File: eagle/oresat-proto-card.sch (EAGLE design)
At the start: 126 parts, among them J1 J-SAMTEC-TFM-110-X1-XXX-D-RA, J2 U.FL, J3 U.FL, J4 U.FL, J6 J-SAMTEC-TFM-120-X1-XXX-D-RA, J7 ORESAT-DEBUG-CONNECTOR-SOLAR, Q1 DMP2240UDM, Q3 MOSFET-PCH-SOT23-6, Q4 MOSFET-PCH-SOT23-6, Q5 PMV45EN, Q6 PMV45EN, U1 TCAN330, U3 MAX7310ATE, U4 MAX4211FETE, U5 TPS62111RSA, U7 STM32F091C, U8 MIC842LYC5, U9 MIC842LYC5, X2 16MHZ-2.5x2mm

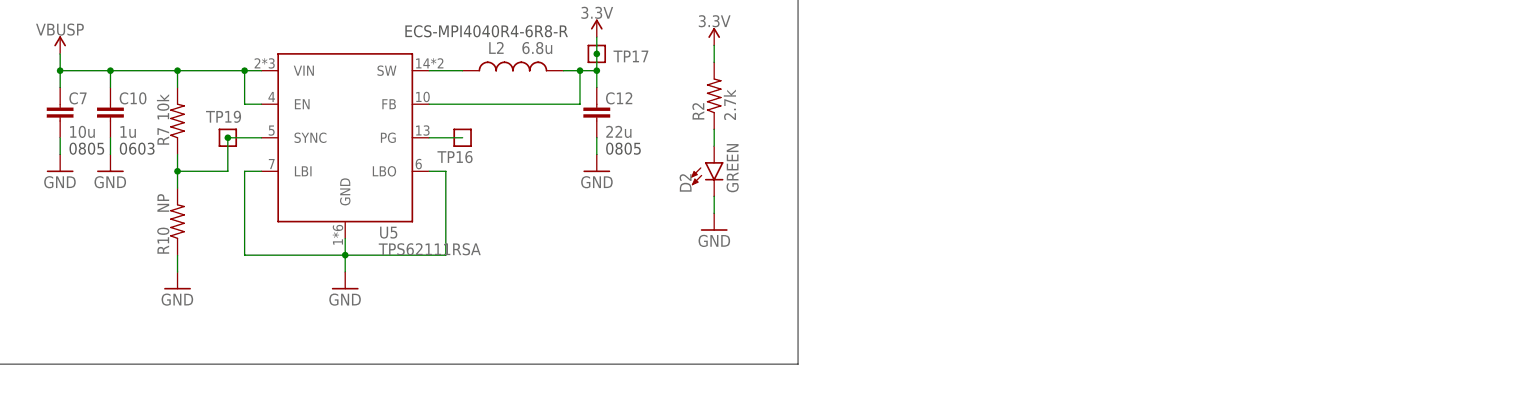
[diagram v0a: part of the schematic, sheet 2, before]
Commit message: swapped 0402 to 0603 where necessary, fixed labels on tnames layer
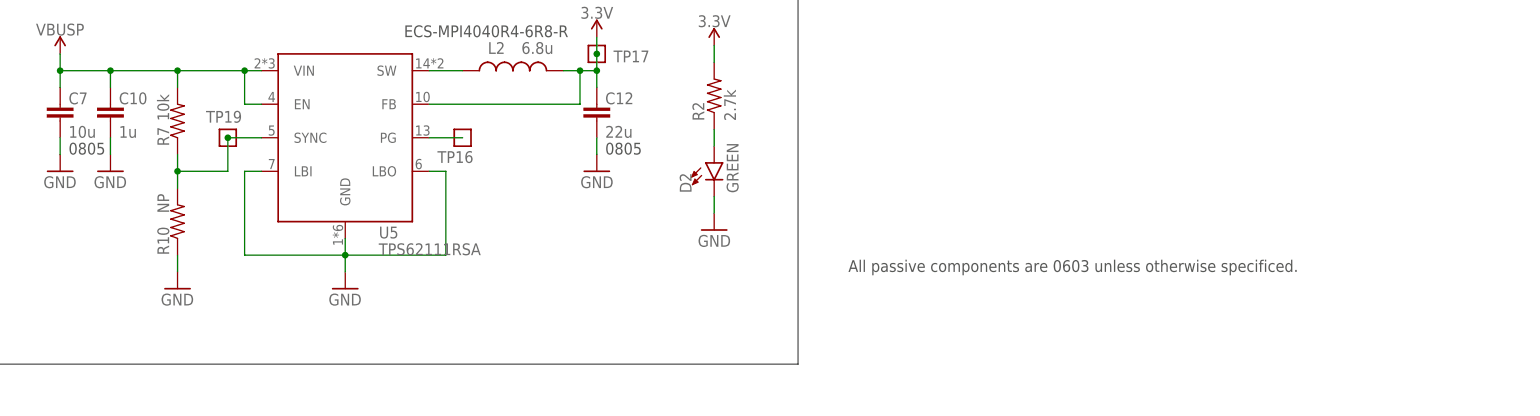
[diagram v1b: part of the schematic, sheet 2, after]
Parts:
- C1, C2: device rcl_custom:C-EU0402-B-NOSILK -> oresat-rcl:C-EU0603-C-NOSILK
- C4, C5, C6: device oresat-rcl:C-EU0603-B-NOSILK -> oresat-rcl:C-EU0603-C-NOSILK
- R10, R11, R12, R13, R14, R15, R16, R18, R19, R20, R21, R22, R23, R25, R26, R27, R28, R30, R31, R32, R33, R34, R35, R36, R37, R38, R39, R40, R41, R42, R43, R44, R5, R6, R7, R8, R9: device rcl_custom:R-US_0402-B-NOSILK -> oresat-rcl:R-US_0603-C-NOSILK
- R29: device rcl:R-US_R1206 -> oresat-rcl:R-US_0603-C-NOSILK
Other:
- note added: "All passive components are 0603 unless otherwise specificed."
- note added: "TODO:Replace attributes of passives with 0603"

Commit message: updated design blocks, got rid of unneeded breakouts
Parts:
- removed C1: 100n, oresat-rcl:C-EU0603-C-NOSILK
- removed C10: 1u, oresat-rcl:C-EU0603-B-NOSILK
- removed C12: 22u, oresat-rcl:C-EU0805-B-NOSILK
- removed C2: NP, oresat-rcl:C-EU0603-C-NOSILK
- removed C4, C5, C6: 1u, oresat-rcl:C-EU0603-C-NOSILK
- removed C7: 10u, oresat-rcl:C-EU0805-B-NOSILK
- removed D1, D2: GREEN, SparkFun-LED:LED-GREEN0603
- removed D4: AMBER, SparkFun-LED:LED-GREEN0603
- removed JP1: (no value), pinhead:PINHD-1X6
- removed JP3: (no value), pinhead:PINHD-1X3
- removed JP5, JP6: (no value), pinhead:PINHD-1X5
- removed JP7: (no value), pinhead:PINHD-2X10
- removed L2: 6.8u, L-ECS-MPI4040:L-ECS-MPI4040
- removed Q1: DMP2240UDM, Q-MOSFET-PCH-dual-SOT23-6:MOSFET-PCH-SOT23-6
- removed Q3, Q4: MOSFET-PCH-SOT23-6, Q-MOSFET-PCH-SOT23-6:MOSFET-PCH-SOT23-6
- removed Q5, Q6: PMV45EN, Tova:PMV45EN
- removed R1, R12, R2: 2.7k, oresat-rcl:R-US_0603-C-NOSILK
- removed R10, R11, R14, R19, R20, R22, R23, R32, R34, R36, R37, R5, R8, R9: NP, oresat-rcl:R-US_0603-C-NOSILK
- removed R15, R26, R27, R28, R30, R35, R38, R42, R7: 10k, oresat-rcl:R-US_0603-C-NOSILK
- removed R16, R43: 330k, oresat-rcl:R-US_0603-C-NOSILK
- removed R18, R44: 1M, oresat-rcl:R-US_0603-C-NOSILK
- removed R25, R41: 100, oresat-rcl:R-US_0603-C-NOSILK
- removed R29: 100m, oresat-rcl:R-US_0603-C-NOSILK
- removed R31, R33: 0, oresat-rcl:R-US_0603-C-NOSILK
- removed R4: 100, rcl_custom:R-US_0402-B-NOSILK
- removed TP1, TP10, TP11, TP12, TP13, TP14, TP16, TP17, TP18, TP19, TP20, TP22, TP3, TP5, TP6, TP7, TP8, TP9: TEST-POINT, Tova:TEST-POINT
- removed U3: MAX7310ATE, U-Maxim-MAX7310-I2C-GPIO-expander:MAX7310
- removed U4: MAX4211FETE, U-Maxim-MAX4211-power-monitor:MAX4211
- removed U5: TPS62111RSA, U-TI-TPS6211x-SPS-buck:TPS6211X
- removed U8, U9: MIC842LYC5, U-Microchip-MIC842-Comparator:MIC842LYC5
- added C11, C17, C22, C23: 1u, oresat-rcl:C-EU0603-C-NOSILK
- added C16: 22u, oresat-rcl:C-EU0805-B-NOSILK
- added C3: 100n, oresat-rcl:C-EU0603-C-NOSILK
- added C8: NP, oresat-rcl:C-EU0603-C-NOSILK
- added C9: 10u, oresat-rcl:C-EU0805-B-NOSILK
- added D3, D6: GREEN, SparkFun-LED:LED-GREEN0603
- added D7: AMBER, SparkFun-LED:LED-GREEN0603
- added JP11, JP8: (no value), pinhead:PINHD-2X10
- added L1: 6.8u, L-ECS-MPI4040:L-ECS-MPI4040
- added Q10: DMP2240UDM, Q-MOSFET-PCH-dual-SOT23-6:MOSFET-PCH-SOT23-6
- added Q2, Q7: MOSFET-PCH-SOT23-6, Q-MOSFET-PCH-SOT23-6:MOSFET-PCH-SOT23-6
- added Q8, Q9: PMV45EN, Tova:PMV45EN
- added R17, R3, R76: 2.7k, oresat-rcl:R-US_0603-C-NOSILK
- added R24: 10, oresat-rcl:R-US_0603-C-NOSILK
- added R46, R52, R53, R55, R56, R57, R59, R67, R69, R71, R72, R75: NP, oresat-rcl:R-US_0603-C-NOSILK
- added R60, R80: 100, oresat-rcl:R-US_0603-C-NOSILK
- added R61, R62, R63, R65, R70, R73, R74, R77, R81: 10k, oresat-rcl:R-US_0603-C-NOSILK
- added R64: 100m, rcl:R-US_R1206
- added R66, R68: 0, oresat-rcl:R-US_0603-C-NOSILK
- added R78, R82: 330k, oresat-rcl:R-US_0603-C-NOSILK
- added R79, R83: 1M, oresat-rcl:R-US_0603-C-NOSILK
- added TP15, TP2, TP21, TP23, TP24, TP33, TP34, TP35, TP36, TP37, TP38, TP39, TP4, TP40, TP41, TP42: TEST-POINT-LARGE-SQUARE, oresat-misc:TEST-POINT-LARGE-SQUARE
- added TP25: TEST-POINT, Tova:TEST-POINT
- added U10: TPS62111RSA, U-TI-TPS6211x-SPS-buck:TPS6211X
- added U11, U12: MIC842LYC5, U-Microchip-MIC842-Comparator:MIC842LYC5
- added U2: MAX7310ATE, U-Maxim-MAX7310-I2C-GPIO-expander:MAX7310
- added U6: MAX4211FETE, U-Maxim-MAX4211-power-monitor:MAX4211
- R39, R40: value 47k -> NP; DPN 311-47.0KLRCT-ND -> 1276-4275-1-ND; MFR Yageo -> Samsung; MPN RC0402FR-0747KL -> RC1005F6653CS
- TP31, TP32: value TEST-POINT -> TEST-POINT-LARGE-SQUARE; device Tova:TEST-POINT -> oresat-misc:TEST-POINT-LARGE-SQUARE
- renumbered R13 to R54, R21 to R58, R6 to R45
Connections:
- removed net CAN_SILENT: U1.S, U7.PA9
- removed net IOUT: R31.2, U4.IOUT
- removed net MAX4211-3V3: C5.1, TP10.1, U3.IO7, U4.VCC
- removed net N$270: D1.A, R1.1
- removed net N$271: D2.A, R2.1
- removed net N$385: R39.1, R40.1, TP5.1, U3.IO6
- removed net N$398: Q3.S, R29.2, R35.2, U4.RS-
- removed net N$400: C6.1, R43.1, R44.1, U8.INP
- removed net N$401: C4.1, R16.1, R18.1, U9.INP
- removed net N$479: Q1.2.S, R41.2
- removed net N$480: Q1.2.G, R42.2, TP22.1, U8.OUT
- removed net N$527: J7.SWO, TP32.1
- removed net N$575: D4.A, R12.1
- removed net N$579: Q1.1.S, R25.2
- removed net N$580: Q1.1.G, R15.2, TP7.1, U9.OUT
- removed net N$589: R26.1, U3.!RESET
- removed net N$590: Q4.G, Q5.D, R27.1
- removed net N$593: Q4.D, R29.1, U4.RS+
- removed net N$596: R31.1, R32.2, TP12.1, U4.CIN1+
- removed net N$597: R33.1, R34.2, TP11.1, U4.CIN1-
- removed net N$599: R33.2, U4.CIN2+, U4.REF
- removed net N$603: C2.1, R36.2, R37.2
- removed net N$604: R37.1, U4.INHIBIT
- removed net POUTPROT: JP7.13, R49.2, U7.PA8
- removed net TPS62111-PG: TP16.1, U5.PG
- removed net TPS62111-SYNC: R10.2, R7.1, TP19.1, U5.SYNC
- removed net TPS62111_SW: L2.1, U5.SW
- new net IOUT1: R66.2, U6.IOUT
- new net N$518: D3.A, R3.1
- new net N$519: D6.A, R17.1
- new net N$520: R61.1, U2.!RESET
- new net N$522: J7.DEBUG-3, TP29.1
- new net N$529: Q7.G, Q8.D, R62.1
- new net N$530: Q7.D, R64.1, U6.RS+
- new net N$531: R66.1, R67.2, TP15.1, U6.CIN1+
- new net N$532: R68.1, R69.2, TP4.1, U6.CIN1-
- new net N$533: R68.2, U6.CIN2+, U6.REF
- new net N$534: R72.1, U6.INHIBIT
- new net N$535: C8.1, R71.2, R72.2
- new net N$536: Q2.S, R64.2, R70.2, U6.RS-
- new net N$537: D7.A, R76.1
- new net N$538: Q10.1.S, R60.2
- new net N$539: Q10.1.G, R77.2, TP41.1, U12.OUT
- new net N$540: TP40.1, U2.IO6
- new net N$541: Q10.2.S, R80.2
- new net N$573: Q10.2.G, R81.2, TP42.1, U11.OUT
- new net N$574: C23.1, R82.1, R83.1, U11.INP
- new net N$578: C22.1, R78.1, R79.1, U12.INP
- new net N$581: TP36.1, U2.IO7
- new net PA8/POUTPROT: JP8.6, R49.2, U7.PA8
- new net PA9/CAN_SILENT: JP8.8, U1.S, U7.PA9
- new net PB10: JP11.10, U7.PB10
- new net PB11: JP11.12, U7.PB11
- new net PB12: JP11.14, U7.PB12
- new net PB13: JP11.16, U7.PB13
- new net PB14: JP11.18, U7.PB14
- new net PB15: JP11.20, U7.PB15
- new net PB2: JP11.13, U7.PB2
- new net PB8: JP11.6, U7.PB8
- new net PB9: JP11.8, U7.PB9
- new net PC13: JP8.1, U7.PC13
- new net PC14: JP8.3, U7.PC14-OSC32_IN
- new net PC15: JP8.5, U7.PC15-OSC32_OUT
- new net TPS62111-PG1: TP32.1, U10.PG
- new net TPS62111-SYNC1: R74.1, R75.2, TP33.1, U10.SYNC
- new net TPS62111_SW3: L1.1, U10.SW
- net !FAULT: now also Q9.D, R73.1, TP24.1, U2.IO2; no longer Q6.D, R38.1, TP8.1, U3.IO2
- net !SD: no longer JP1.3
- net 3.3V: now also C16.1, L1.2, R17.2, TP34.1, U10.FB; no longer C12.1, JP1.4, JP5.1, JP5.2, JP5.3, JP5.4, JP5.5, JP6.1, JP6.2, JP6.3, JP6.4, JP6.5, L2.2, R2.2, TP17.1, U5.FB
- net AD0: now also R39.1, R40.2, R46.1, U2.AD0; no longer R5.1, R8.2, R9.1, U3.AD0
- net AD1: now also R52.1, R53.2, R55.1, U2.AD1; no longer R11.1, R14.2, R19.1, U3.AD1
- net AD2: now also R56.1, R57.2, R59.1, U2.AD2; no longer R20.1, R22.2, R23.1, U3.AD2
- net BOOT0: now also JP11.3, TP25.1, U2.IO5; no longer TP26.1, U3.IO5
- net CAN1_H: no longer JP1.1
- net CAN1_L: no longer JP1.2
- net CAN_RX: now also JP8.12
- net CAN_SHDN: now also JP8.10
- net CAN_TX: now also JP8.14
- net CB-RESET: now also R65.2, TP23.1, U2.IO4, U6.CIN2-; no longer R30.2, TP14.1, U3.IO4, U4.CIN2-
- net CB_CTRL: now also Q2.G, Q9.G, R70.1, TP39.1, U6.COUT1, U6.COUT2, U6.LE; no longer Q3.G, Q6.G, R35.1, TP3.1, U4.COUT1, U4.COUT2, U4.LE
- net GND: now also C11.2, C16.2, C17.2, C22.2, C23.2, C3.1, C9.2, D3.C, D6.C, D7.C, JP8.19, Q8.S, Q9.S, R45.1, R54.1, R58.1, R63.1, R65.1, R67.1, R69.1, R71.1, R75.1, R77.1, R81.1, U10.GND, U10.LBI, U10.LBO, U11.GND, U12.GND, U2.GND, U6.GND; no longer C1.1, C10.2, C12.2, C4.2, C5.2, C6.2, C7.2, D1.C, D2.C, D4.C, JP1.6, JP7.15, JP7.17, JP7.19, Q5.S, Q6.S, R10.1, R14.1, R15.1, R22.1, R28.1, R30.1, R32.1, R34.1, R36.1, R42.1, R8.1, U3.GND, U4.GND, U5.GND, U5.LBI, U5.LBO, U8.GND, U9.GND
- net N$523: now also J7.DEBUG-2, TP28.1; no longer J7.DEBUG-3, TP31.1
- net N$524: now also J7.DEBUG-1, TP27.1; no longer J7.DEBUG-2, TP30.1
- net N$525: now also J7.DEBUG-0, TP26.1; no longer J7.DEBUG-1, TP29.1
- net N$526: now also J7.SWO, TP30.1; no longer J7.DEBUG-0, TP28.1
- net NRESET: now also JP11.1; no longer TP27.1
- net ON/!OFF: now also C17.1, Q8.G, R63.2, R76.2, TP21.1, U2.IO3, U6.VCC; no longer Q5.G, R12.2, R28.2, TP13.1, U3.IO3
- net OPD_PWR: now also R24.1; no longer R4.1
- net OPD_SCL: now also R80.1; no longer R41.1
- net OPD_SDA: now also R60.1; no longer R25.1
- net PA0: now also JP8.7; no longer JP7.2
- net PA1: now also JP8.9; no longer JP7.4
- net PA15: now also JP8.16; no longer JP7.11
- net PA2/USART2_TX: now also JP8.11; no longer JP7.6
- net PA3/USART2_RX: now also JP8.13; no longer JP7.8
- net PA4: now also JP8.15; no longer JP7.10
- net PA5/SPI1_SCK: now also JP8.17; no longer JP7.12
- net PA6/SPI1_MISO: now also JP8.2; no longer JP7.14
- net PA7/SPI1_MOSI: now also JP8.4; no longer JP7.16
- net PB0: now also JP11.9; no longer JP7.18
- net PB1: now also JP11.11; no longer JP7.20
- net PB3: now also JP11.15; no longer JP7.9
- net PB4: now also JP11.17; no longer JP7.7
- net PB5: now also JP11.19; no longer JP7.5
- net PB6/SCL: now also JP11.2, U2.IO0; no longer JP7.3, R40.2, U3.IO0
- net PB7/SDA: now also JP11.4, U2.IO1; no longer JP7.1, R39.2, U3.IO1
- net PEN-SCL-FILT: now also Q10.2.D, R40.1, R53.1, R57.1, R82.2, TP37.1, U2.SCL; no longer Q1.2.D, R43.2, R45.1, R54.1, R58.1, TP18.1, U3.SCL
- net PEN-SDA-FILT: now also Q10.1.D, R46.2, R55.2, R59.2, R78.2, TP38.1, U2.SDA; no longer Q1.1.D, R16.2, R19.2, R23.2, R9.2, TP20.1, U3.SDA
- net POUT: now also TP2.1, U6.POUT; no longer TP6.1, U4.POUT
- net SWCLK: now also JP11.7
- net SWDIO: now also JP11.5
- net VBUS: now also Q7.S, R62.2; no longer Q4.S, R27.2
- net VBUSP: now also C11.1, C8.2, C9.1, Q2.D, R3.2, R74.2, TP31.1, U10.EN, U10.VIN; no longer C10.1, C2.2, C7.1, JP1.5, JP3.1, JP3.2, JP3.3, Q3.D, R1.2, R7.2, TP9.1, U5.EN, U5.VIN
- net VPD: now also C3.2, R24.2, R39.2, R52.2, R56.2, R61.2, R73.2, R79.2, R83.2, TP35.1, U11.VDD, U12.VDD, U2.V+; no longer C1.2, R11.2, R18.2, R20.2, R26.2, R38.2, R4.2, R44.2, R5.2, TP1.1, U3.V+, U8.VDD, U9.VDD
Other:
- note added: "1206"
- note added: "GPIO Breakouts"
- note added: "Rx-Tx switch happens on programming board"
- note added: "TODO: Replace with part in OreSat-Eagle Repo"
- note added: "VBAT not bypassed becase not enough room instead tied into nearest bypass cap"
- note removed: "0603"
- note removed: "47k forces slow I2C"
- note removed: "Place only if I2C pullups not placed."
- note removed: "Rx-Tx flip happens on proramming board"
- note removed: "TODO:Replace attributes of passives with 0603"
- note removed: "Vbat not bypassed because no space on layout tied to nearest bypass cap instead"

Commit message: Polishing to the schematic only; ready for v4! Still needs layout polishing.
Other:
- note added: "3.4"
- note added: "4.0"
- note added: "All caps are 0603 ceramic 10% X5R Vw>=16V unless marked"
- note added: "All resistors 0603 +/- 1% unless marked"
- note removed: "3.1"
- note removed: "All caps are 0402 ceramic 10% X5R Vw>=16V unless marked"
- note removed: "All resistors 0402 +/- 1% unless marked"
- note removed: "TODO: Replace with part in OreSat-Eagle Repo"
- moved on the sheet: C19, R48, U1

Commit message: moved ffc to bottom of card, fixed silkscreen, moved and expanded Vbus and 3.3V breakouts
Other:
- note added: "All caps are 0402 ceramic 10% X5R Vw>=16V unless marked"
- note added: "All caps are ceramic 10% X5R >= 16V V unless marked"
- note added: "All resistors 0402 +/- 1% unless marked"
- note removed: "3.4"
- note removed: "All caps are 0603 ceramic 10% X5R Vw>=16V unless marked"
- note removed: "All passive components are 0603 unless otherwise specificed."
- note removed: "Each VDD pin bypassed"
- moved on the sheet: C19, R48, U1

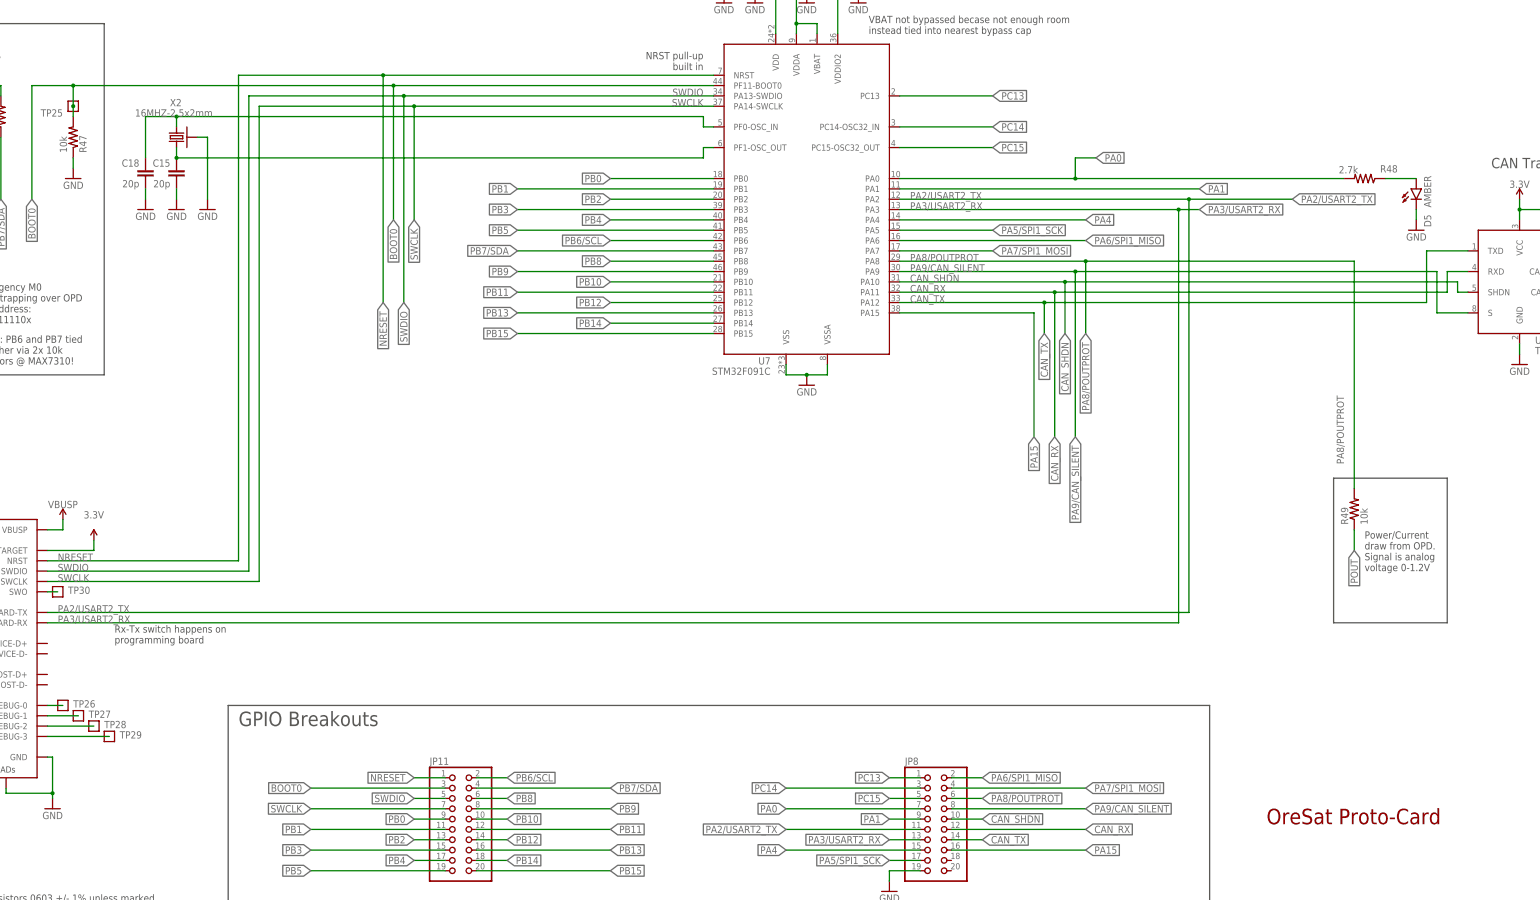
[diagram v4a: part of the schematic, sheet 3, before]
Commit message: fixed an error where Pout was not routed to an ADC pin
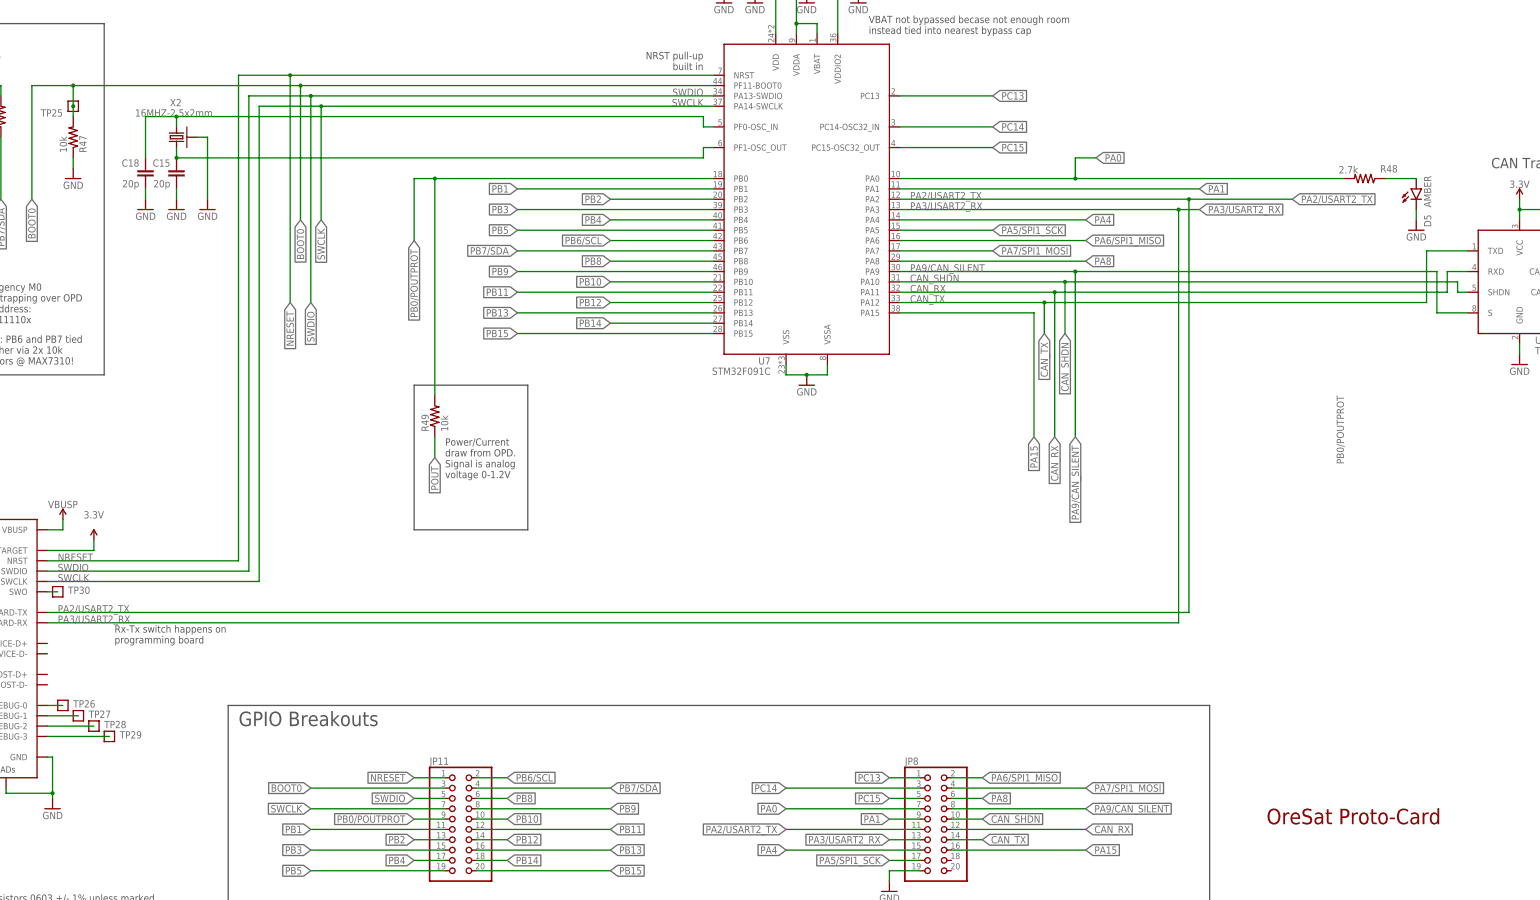
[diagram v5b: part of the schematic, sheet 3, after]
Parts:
- C11, C17, C22, C23: DPN 311-1446-1-ND -> 311-1444-1-ND; MPN CC0603KRX7R7BB105 -> CC0603KRX5R7BB105
- C3: DPN 1276-1001-1-ND -> 399-14941-1-ND; MFR Samsung -> Kemet; MPN CL05B104KO5NNNC -> C0603C104K4PAC7867
- R17, R3, R76: DPN A129632CT-ND -> P2.7KDBCT-ND; MFR TE Connectivity -> Panasonic; MPN CRGCQ0402F2K7 -> ERA-3AEB272V
- R24: DPN 311-100LRCT-ND -> 311-10.0HRCT-ND; MPN RC0402FR-07100RL -> RC0603FR-0710RL
- R60, R80: DPN 311-100LRCT-ND -> 311-100HRCT-ND; MPN RC0402FR-07100RL -> RC0603FR-07100RL
- R61, R62, R63, R65, R70, R73, R74, R77, R81: DPN 311-10.0KLRCT-ND -> RNCP0603FTD10K0CT-ND; MFR Yageo -> Stackpole; MPN RC0402FR-0710KL -> RNCP0603FTD10K0
- R66, R68: DPN 311-0.0JRCT-ND -> 311-0.0GRCT-ND; MPN RC0402JR-070RL -> RC0603JR-070RL
- R78, R82: DPN 749-1575-1-ND -> A129718CT-ND; MFR Vishay -> TE Connectivity; MPN MCS04020C3303FE000 -> CRGCQ0603F330K
- R79, R83: DPN 311-1.00MLRCT-ND -> 311-1.00MHRCT-ND; MPN RC0402FR-071ML -> RC0603FR-071ML
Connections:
- removed net PA8/POUTPROT: JP8.6, R49.2, U7.PA8
- removed net PB0: JP11.9, U7.PB0
- new net PA8: JP8.6, U7.PA8
- new net PB0/POUTPROT: JP11.9, R49.2, U7.PB0
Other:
- moved on the sheet: R49

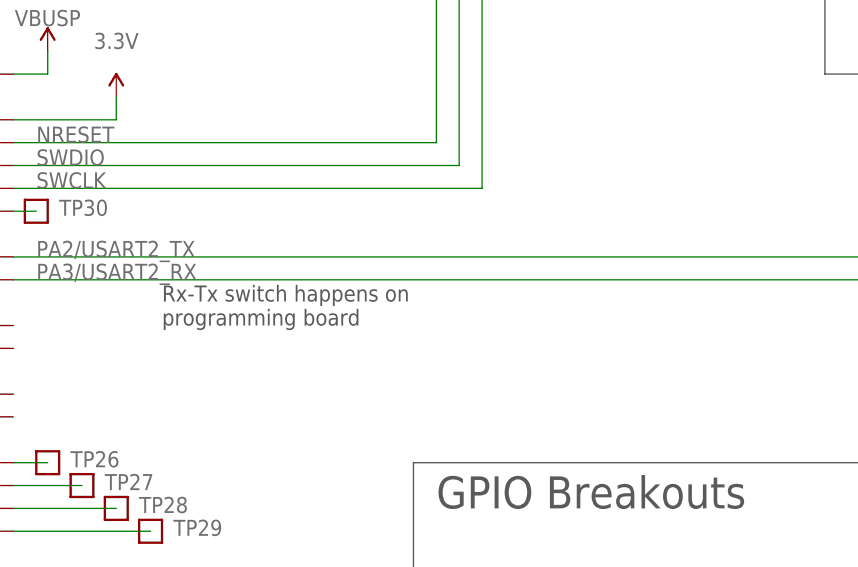
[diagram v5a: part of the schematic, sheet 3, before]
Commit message: Minor DRC clean up, fixed 3.3V plane cut by VBUSP, and some TSTOPs being too close.
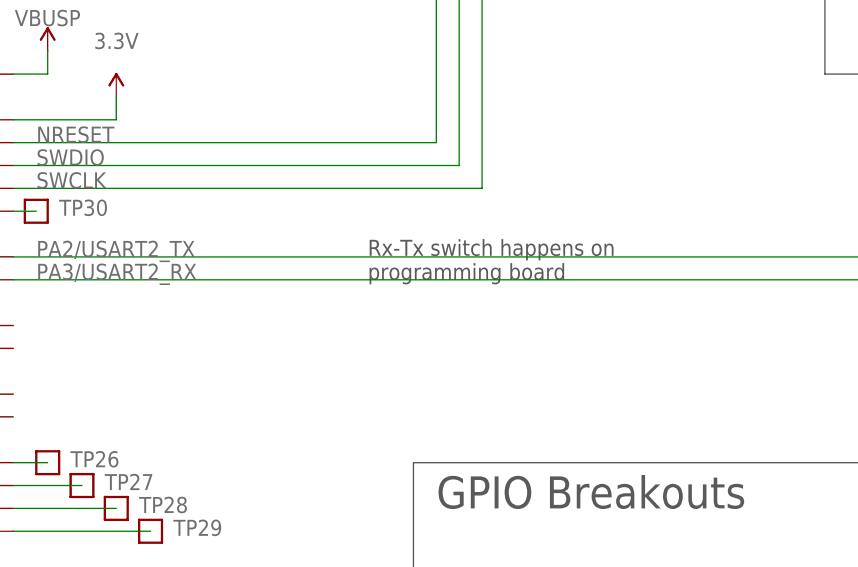
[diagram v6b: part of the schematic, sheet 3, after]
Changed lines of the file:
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@@
 <?xml version="1.0" encoding="utf-8"?>
 <!DOCTYPE eagle SYSTEM "eagle.dtd">
-<eagle version="9.6.2">
+<eagle version="9.6.1">
 <drawing>
 <settings>
@@
 <text x="233.68" y="220.98" size="1.778" layer="97">VBAT not bypassed becase not enough room
 instead tied into nearest bypass cap</text>
-<text x="48.26" y="71.12" size="1.778" layer="97">Rx-Tx switch happens on
+<text x="71.12" y="76.2" size="1.778" layer="97">Rx-Tx switch happens on
 programming board</text>
 <wire x1="76.2" y1="5.08" x2="76.2" y2="55.88" width="0.1524" layer="97"/>
